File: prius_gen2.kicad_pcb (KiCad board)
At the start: 4 copper layers, 130.6 x 65 mm, 143 parts, among them J1 Conn_02x05_Odd_Even, J2 Conn_01x06, J3 Conn_01x23, J4 Conn_01x14, Q1 Q_NPN_BEC, Q2 Q_PNP_BEC, Q3 Q_NPN_BEC, Q4 Q_PNP_BEC, SW1 SW_Push, SW2 SW_Push, U1 STM32F407VETx, U2 ULN2003A, U3 AD2S1205YSTZ, U4 TJA1051T-3, U5 LMR14020, U6 AZ1117-3.3, U7 MCP602, U8 AD8676xR, Y1 8MHz, Y2 8.192MHz

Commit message: v0.4 manufactoring files
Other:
- board text added: "Prius G2 rev 4 2023-01"
- board text removed: "Prius G2 rev 4 2022-12"
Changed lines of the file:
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@@
   (setup
     (pad_to_mask_clearance 0)
-    (solder_mask_min_width 0.25)
     (pcbplotparams
       (layerselection 0x0000010_7ffffff8)
@@
     (effects (font (size 1 1) (thickness 0.15)) (justify mirror))
   )
-  (gr_text "Prius G2 rev 4\n2022-12" (at 165.777 71.7995 180) (layer "B.SilkS")
+  (gr_text "Prius G2 rev 4\n2023-01" (at 165.777 71.7995 180) (layer "B.SilkS")
     (effects (font (size 1.25 1.25) (thickness 0.3)) (justify mirror))
   )

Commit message: fixes for v5
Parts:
- removed J1: Conn_02x05_Odd_Even, Connector_PinHeader_1.27mm:PinHeader_2x05_P1.27mm_Vertical_SMD
- added C26: 2.2uF, Capacitor_SMD:C_0603_1608Metric, F.Cu at (148.1, 83.7)
- added C27: 2.2uF, Capacitor_SMD:C_0603_1608Metric, F.Cu at (163.7, 87.6)
- added TP8: TestPoint, TestPoint:TestPoint_Keystone_5000-5004_Miniature, B.Cu at (176.2, 91.0)
- added TP9: TestPoint, TestPoint:TestPoint_Keystone_5000-5004_Miniature, B.Cu at (176.2, 87.8)
- J5: moved to B.Cu
- moved R14 43.7 mm to (143.8, 78.9), turned to 90 degrees
- moved C16 41.5 mm to (143.8, 81.5), turned to -90 degrees
- moved J5 37.4 mm to (146.2, 70.5), turned to 180 degrees
- moved U9 37.2 mm to (142.1, 74.4)
- moved D11 36.9 mm to (142.1, 70.4), turned to 0 degrees
- moved C11 1.83 mm to (146.5, 83.7)
- moved C10 0.74 mm to (165.2, 87.6)
- moved R3 0.27 mm to (161.3, 86.5)
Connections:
- U1 pad 49: unconnected-(U1-Pad49) -> Net-(U1-VCAP_1)
- U1 pad 6: unconnected-(U1-Pad6) -> +3V3
- U1 pad 73: unconnected-(U1-Pad73) -> Net-(U1-VCAP_2)
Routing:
- net /UART3_RX: track 0.00 -> 17.3 mm
- net /UART3_TX: track 0.00 -> 16.2 mm
- net /USB_D+: track 33.7 -> 20.5 mm, vias 2 -> 0
- net GND: track 67.2 -> 54.6 mm, vias 75 -> 87
- net /USB_D-: track 34.6 -> 22.3 mm, vias 2 -> 0
- net /nRESET: track 86.1 -> 77.9 mm
- net +5V: track 265.2 -> 259.1 mm
- net Net-(U1-VCAP_1): track 0.00 -> 5.88 mm
- net Net-(U1-VCAP_2): track 0.00 -> 4.42 mm
- net /SWCLK: track 24.6 -> 21.3 mm, vias 1 -> 3
- net /SWDIO: track 22.1 -> 19.1 mm
- net +3V3: track 212.1 -> 214.5 mm
- net Net-(U1-BOOT0): track 40.5 -> 39.2 mm
- net /TIM1_BKIN: track 36.2 -> 37.0 mm
- net Net-(D11-A): track 9.10 -> 9.47 mm, vias 2 -> 0
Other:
- board text added: "Prius G2 rev 5 2023-02"
- board text removed: "Prius G2 rev 4 2023-01"

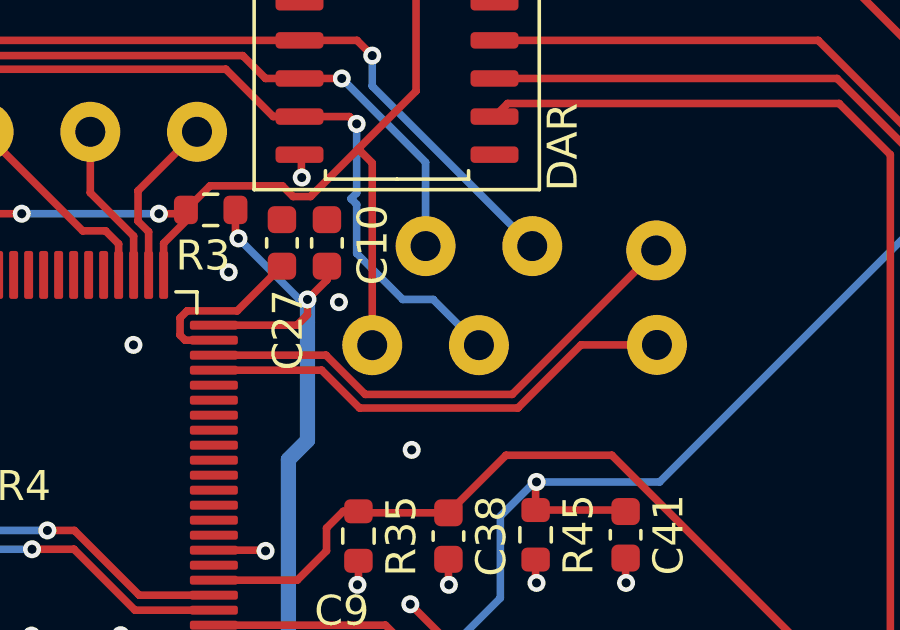
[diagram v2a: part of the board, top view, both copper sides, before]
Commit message: fixed some drc errors
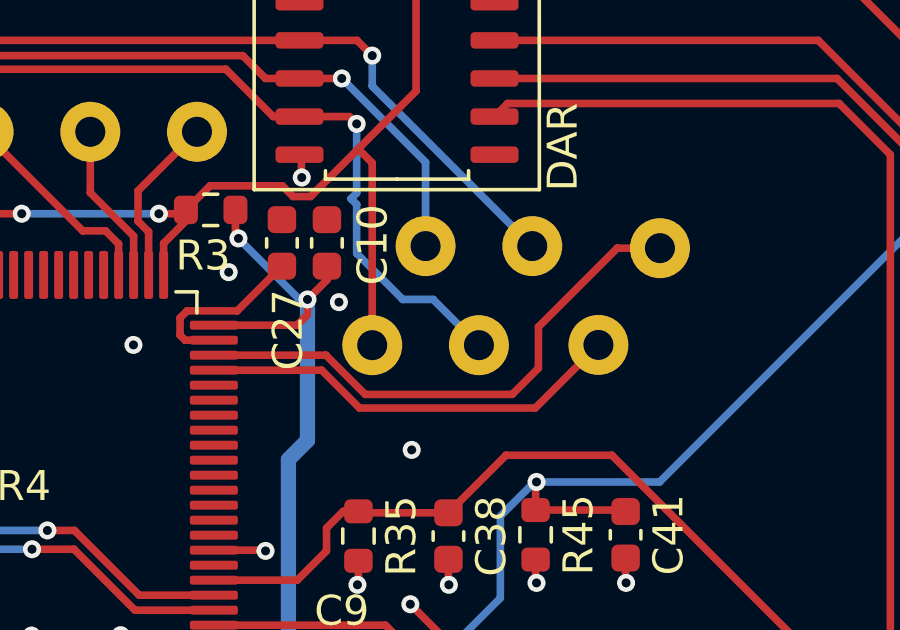
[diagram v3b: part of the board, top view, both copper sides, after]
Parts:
- moved TP8 1.95 mm to (174.2, 91.0)
- moved TP9 0.15 mm to (176.3, 87.8)
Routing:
- net /UART3_TX: track 16.2 -> 14.2 mm
- net /UART3_RX: track 17.3 -> 18.2 mm
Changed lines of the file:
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@@
   )
   (footprint "TestPoint:TestPoint_Keystone_5000-5004_Miniature" (layer "B.Cu")
-    (at 176.15 87.825 180)
+    (at 176.275 87.75 180)
     (descr "Keystone Miniature THM Test Point 5000-5004, http://www.keyelco.com/product-pdf.cfm?p=1309")
     (tags "Through Hole Mount Test Points")
@@
   )
   (footprint "TestPoint:TestPoint_Keystone_5000-5004_Miniature" (layer "B.Cu")
-    (at 176.175 90.975 180)
+    (at 174.225 90.975 180)
     (descr "Keystone Miniature THM Test Point 5000-5004, http://www.keyelco.com/product-pdf.cfm?p=1309")
     (tags "Through Hole Mount Test Points")
@@
   (segment (start 157.287 85.9035) (end 157.287 83.8715) (width 0.254) (layer "F.Cu") (net 55))
   (segment (start 158.731 87.3475) (end 157.287 85.9035) (width 0.254) (layer "F.Cu") (net 55))
-  (segment (start 171.35 92.625) (end 176.15 87.825) (width 0.254) (layer "F.Cu") (net 56))
-  (segment (start 165.142338 91.3175) (end 166.449838 92.625) (width 0.254) (layer "F.Cu") (net 56))
-  (segment (start 166.449838 92.625) (end 171.35 92.625) (width 0.254) (layer "F.Cu") (net 56))
-  (segment (start 161.406 91.3175) (end 165.142338 91.3175) (width 0.254) (layer "F.Cu") (net 56))
-  (segment (start 176.175 90.975) (end 173.642052 90.975) (width 0.254) (layer "F.Cu") (net 57))
-  (segment (start 171.538052 93.079) (end 166.261786 93.079) (width 0.254) (layer "F.Cu") (net 57))
-  (segment (start 165.000286 91.8175) (end 161.406 91.8175) (width 0.254) (layer "F.Cu") (net 57))
-  (segment (start 166.261786 93.079) (end 165.000286 91.8175) (width 0.254) (layer "F.Cu") (net 57))
-  (segment (start 173.642052 90.975) (end 171.538052 93.079) (width 0.254) (layer "F.Cu") (net 57))
+  (segment (start 171.35 92.625) (end 166.449838 92.625) (width 0.254) (layer "F.Cu") (net 56))
+  (segment (start 172.225 90.375) (end 172.225 91.75) (width 0.254) (layer "F.Cu") (net 56))
+  (segment (start 172.225 91.75) (end 171.35 92.625) (width 0.254) (layer "F.Cu") (net 56))
+  (segment (start 174.85 87.75) (end 172.225 90.375) (width 0.254) (layer "F.Cu") (net 56))
+  (segment (start 165.142338 91.3175) (end 161.406 91.3175) (width 0.254) (layer "F.Cu") (net 56))
+  (segment (start 166.449838 92.625) (end 165.142338 91.3175) (width 0.254) (layer "F.Cu") (net 56))
+  (segment (start 176.275 87.75) (end 174.85 87.75) (width 0.254) (layer "F.Cu") (net 56))
+  (segment (start 172.121 93.079) (end 174.225 90.975) (width 0.254) (layer "F.Cu") (net 57))
+  (segment (start 165.000286 91.8175) (end 166.261786 93.079) (width 0.254) (layer "F.Cu") (net 57))
+  (segment (start 166.261786 93.079) (end 172.121 93.079) (width 0.254) (layer "F.Cu") (net 57))
+  (segment (start 161.406 91.8175) (end 165.000286 91.8175) (width 0.254) (layer "F.Cu") (net 57))
   (segment (start 184.86352 84.135968) (end 184.86352 90.03852) (width 0.254) (layer "F.Cu") (net 58))
   (segment (start 188.6345 93.8095) (end 195.323 93.8095) (width 0.254) (layer "F.Cu") (net 58))

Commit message: more updates for v0.5 prod
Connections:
- U1 pad 65: unconnected-(U1-PC8-Pad65) -> Net-(D1-K)
- U1 pad 77: unconnected-(U1-PA15-Pad77) -> Net-(D2-K)
- U1 pad 78: Net-(D1-K) -> /SCLK
- U1 pad 79: unconnected-(U1-PC11-Pad79) -> /MISO
- U1 pad 80: Net-(D2-K) -> unconnected-(U1-PC12-Pad80)
- U1 pad 89: /SCLK -> unconnected-(U1-PB3-Pad89)
- U1 pad 90: /MISO -> unconnected-(U1-PB4-Pad90)
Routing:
- net Net-(D1-K): track 7.42 -> 13.6 mm, vias 0 -> 2
- net /SCLK: track 13.7 -> 17.7 mm
- net /MISO: track 13.9 -> 17.8 mm
- net Net-(D2-K): track 3.20 -> 3.86 mm
